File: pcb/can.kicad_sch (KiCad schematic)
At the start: 3 parts, among them IC5 MCP2551

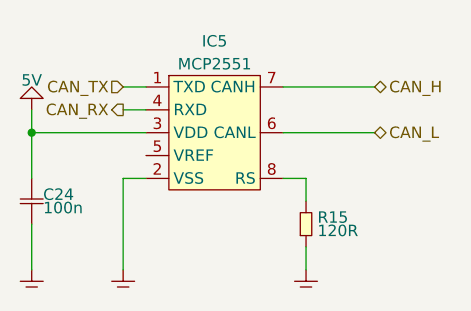
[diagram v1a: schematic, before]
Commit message: changed CAN driver
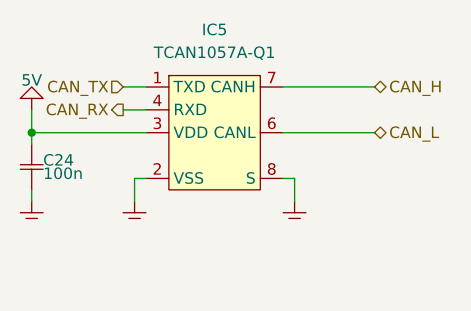
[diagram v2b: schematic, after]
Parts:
- removed R15: 120R, SMT:0603, symbol generic:R
- IC5: value MCP2551 -> TCAN1057A-Q1; footprint SOP:SO-8 -> TSOT:TSOT-23-8; symbol serial:MCP2551 -> serial:TCAN1057A-Q1; DigiKey MCP2551T-I/SNCT-ND -> 296-TCAN1057AVDDFRQ1CT-ND; MPN MCP2551T-I/SN -> TCAN1057AVDDFRQ1; Manufacturer Microchip -> Texas Instruments
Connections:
- net GND: now also IC5.8 (S)
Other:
- moved on the sheet: C24
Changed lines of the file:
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@@
 	(wire
 		(pts
-			(xy 139.7 111.76) (xy 137.16 111.76)
+			(xy 139.7 111.76) (xy 138.43 111.76)
 		)
 		(stroke
@@
 	(wire
 		(pts
-			(xy 154.94 111.76) (xy 157.48 111.76)
+			(xy 127 107.95) (xy 127 106.68)
+		)
+		(stroke
+			(width 0)
+			(type default)
+		)
+	)
+	(wire
+		(pts
+			(xy 156.21 111.76) (xy 154.94 111.76)
 		)
 		(stroke
@@
 	(wire
 		(pts
-			(xy 157.48 119.38) (xy 157.48 121.92)
-		)
-		(stroke
-			(width 0)
-			(type default)
-		)
-	)
-	(wire
-		(pts
 			(xy 137.16 104.14) (xy 139.7 104.14)
 		)
@@
 	(wire
 		(pts
-			(xy 127 116.84) (xy 127 121.92)
-		)
-		(stroke
-			(width 0)
-			(type default)
-		)
-	)
-	(wire
-		(pts
-			(xy 137.16 111.76) (xy 137.16 121.92)
+			(xy 127 113.03) (xy 127 114.3)
+		)
+		(stroke
+			(width 0)
+			(type default)
+		)
+	)
+	(wire
+		(pts
+			(xy 138.43 111.76) (xy 138.43 114.3)
 		)
 		(stroke
@@
 	(wire
 		(pts
-			(xy 127 106.68) (xy 127 111.76)
-		)
-		(stroke
-			(width 0)
-			(type default)
-		)
-	)
-	(wire
-		(pts
-			(xy 157.48 111.76) (xy 157.48 114.3)
+			(xy 156.21 111.76) (xy 156.21 114.3)
 		)
 		(stroke
@@
 	(symbol
 		(lib_id "generic:GND")
-		(at 137.16 121.92 0)
+		(at 138.43 114.3 0)
 		(unit 1)
 		(exclude_from_sim no)
@@
 		(fields_autoplaced yes)
 		(property "Reference" "#GND030"
-			(at 140.97 120.65 0)
+			(at 142.24 113.03 0)
 			(effects
 				(font
@@
 		)
 		(property "Value" "GND"
-			(at 140.97 121.92 0)
+			(at 142.24 114.3 0)
 			(effects
 				(font
@@
 		)
 		(property "Footprint" ""
-			(at 137.16 121.92 0)
+			(at 138.43 114.3 0)
 			(effects
 				(font
@@
 		)
 		(property "Datasheet" ""
-			(at 137.16 121.92 0)
+			(at 138.43 114.3 0)
 			(effects
 				(font
@@
 		)
 		(property "Description" ""
-			(at 137.16 121.92 0)
+			(at 138.43 114.3 0)
 			(effects
 				(font
@@
 	(symbol
 		(lib_id "generic:GND")
-		(at 157.48 121.92 0)
+		(at 156.21 114.3 0)
 		(unit 1)
 		(exclude_from_sim no)
@@
 		(fields_autoplaced yes)
 		(property "Reference" "#GND029"
-			(at 161.29 120.65 0)
+			(at 160.02 113.03 0)
 			(effects
 				(font
@@
 		)
 		(property "Value" "GND"
-			(at 161.29 121.92 0)
+			(at 160.02 114.3 0)
 			(effects
 				(font
@@
 		)
 		(property "Footprint" ""
-			(at 157.48 121.92 0)
+			(at 156.21 114.3 0)
 			(effects
 				(font
@@
 		)
 		(property "Datasheet" ""
-			(at 157.48 121.92 0)
+			(at 156.21 114.3 0)
 			(effects
 				(font
@@
 		)
 		(property "Description" ""
-			(at 157.48 121.92 0)
+			(at 156.21 114.3 0)
 			(effects
 				(font
@@
 	)
 	(symbol
-		(lib_id "generic:R")
-		(at 157.48 116.84 90)
-		(unit 1)
-		(exclude_from_sim no)
-		(in_bom yes)
-		(on_board yes)
-		(dnp no)
-		(property "Reference" "R15"
-			(at 158.75 116.84 90)
-			(effects
-				(font
-					(size 1.27 1.27)
-				)
-				(justify right top)
-			)
-		)
-		(property "Value" "120R"
-			(at 158.75 116.84 90)
-			(effects
-				(font
-					(size 1.27 1.27)
-				)
-				(justify right bottom)
-			)
-		)
-		(property "Footprint" "SMT:0603"
-			(at 158.115 119.38 0)
-			(effects
-				(font
-					(size 1.27 1.27)
-				)
-				(hide yes)
-			)
-		)
-		(property "Datasheet" ""
-			(at 157.48 116.84 0)
-			(effects
-				(font
-					(size 1.27 1.27)
-				)
-				(hide yes)
-			)
-		)
-		(property "Description" ""
-			(at 157.48 116.84 0)
-			(effects
-				(font
-					(size 1.27 1.27)
-				)
-				(hide yes)
-			)
-		)
-		(pin "1"
-		)
-		(pin "2"
-		)
-		(instances
-			(project "pcb"
-				(path "/6bb3bad6-1a89-4624-b34d-6ddda7dd16d2/fdb1a2c0-3d58-431c-bfc9-dd28e6008cdb"
-					(reference "R15")
-					(unit 1)
-				)
-			)
-		)
-	)
-	(symbol
 		(lib_id "generic:GND")
-		(at 127 121.92 0)
+		(at 127 114.3 0)
 		(unit 1)
 		(exclude_from_sim no)
@@
 		(fields_autoplaced yes)
 		(property "Reference" "#GND031"
-			(at 130.81 120.65 0)
+			(at 130.81 113.03 0)
 			(effects
 				(font
@@
 		)
 		(property "Value" "GND"
-			(at 130.81 121.92 0)
+			(at 130.81 114.3 0)
 			(effects
 				(font
@@
 		)
 		(property "Footprint" ""
-			(at 127 121.92 0)
+			(at 127 114.3 0)
 			(effects
 				(font
@@
 		)
 		(property "Datasheet" ""
-			(at 127 121.92 0)
+			(at 127 114.3 0)
 			(effects
 				(font
@@
 		)
 		(property "Description" ""
-			(at 127 121.92 0)
+			(at 127 114.3 0)
 			(effects
 				(font
@@
 	)
 	(symbol
-		(lib_id "serial:MCP2551")
+		(lib_id "serial:TCAN1057A-Q1")
 		(at 147.32 106.68 0)
 		(unit 1)
@@
 		(fields_autoplaced yes)
 		(property "Reference" "IC5"
-			(at 147.32 96.52 0)
-			(effects
-				(font
-					(size 1.27 1.27)
-				)
-			)
-		)
-		(property "Value" "MCP2551"
-			(at 147.32 99.06 0)
-			(effects
-				(font
-					(size 1.27 1.27)
-				)
-			)
-		)
-		(property "Footprint" "SOP:SO-8"
+			(at 147.32 95.25 0)
+			(effects
+				(font
+					(size 1.27 1.27)
+				)
+			)
+		)
+		(property "Value" "TCAN1057A-Q1"
+			(at 147.32 97.79 0)
+			(effects
+				(font
+					(size 1.27 1.27)
+				)
+			)
+		)
+		(property "Footprint" "TSOT:TSOT-23-8"
 			(at 165.1 91.44 0)
 			(effects
@@
 			)
 		)
-		(property "Datasheet" "https://ww1.microchip.com/downloads/en/DeviceDoc/20001667G.pdf"
+		(property "Datasheet" "https://www.ti.com/lit/ds/symlink/tcan1057a-q1.pdf"
 			(at 165.1 91.44 0)
 			(effects
@@
 			)
 		)
-		(property "MPN" "MCP2551T-I/SN"
+		(property "MPN" "TCAN1057AVDDFRQ1"
 			(at 165.1 91.44 0)
 			(effects
@@
 			)
 		)
-		(property "Manufacturer" "Microchip"
+		(property "Manufacturer" "Texas Instruments"
 			(at 165.1 91.44 0)
 			(effects
@@
 			)
 		)
-		(property "DigiKey" "MCP2551T-I/SNCT-ND"
+		(property "DigiKey" "296-TCAN1057AVDDFRQ1CT-ND"
 			(at 165.1 91.44 0)
 			(effects
@@
 		)
 		(pin "4"
-		)
-		(pin "5"
 		)
 		(pin "6"
@@
 	(symbol
 		(lib_id "generic:C")
-		(at 127 114.3 0)
+		(at 127 110.49 0)
 		(unit 1)
 		(exclude_from_sim no)
@@
 		(dnp no)
 		(property "Reference" "C24"
-			(at 128.27 114.3 0)
+			(at 128.27 110.49 0)
 			(effects
 				(font
@@
 		)
 		(property "Value" "100n"
-			(at 128.27 114.3 0)
+			(at 128.27 110.49 0)
 			(effects
 				(font
@@
 		)
 		(property "Footprint" "SMT:0603"
-			(at 127 116.84 0)
+			(at 127 113.03 0)
 			(effects
 				(font
@@
 		)
 		(property "Datasheet" ""
-			(at 127 114.3 0)
+			(at 127 110.49 0)
 			(effects
 				(font
@@
 		)
 		(property "Description" ""
-			(at 127 114.3 0)
-			(effects
-				(font
+			(at 127 110.49 0)
+			(effects
+				(font
